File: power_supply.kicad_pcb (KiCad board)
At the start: 2 copper layers, 30 parts, among them J2 Conn_01x03_Socket, J3 Conn_01x02_Socket, J4 Conn_01x03_Socket, U1 LM317_TO-220, U2 LM337_TO220, U3 LM385BZ-1.2, U4 LM385BZ-1.2, U5 LM7812_TO220

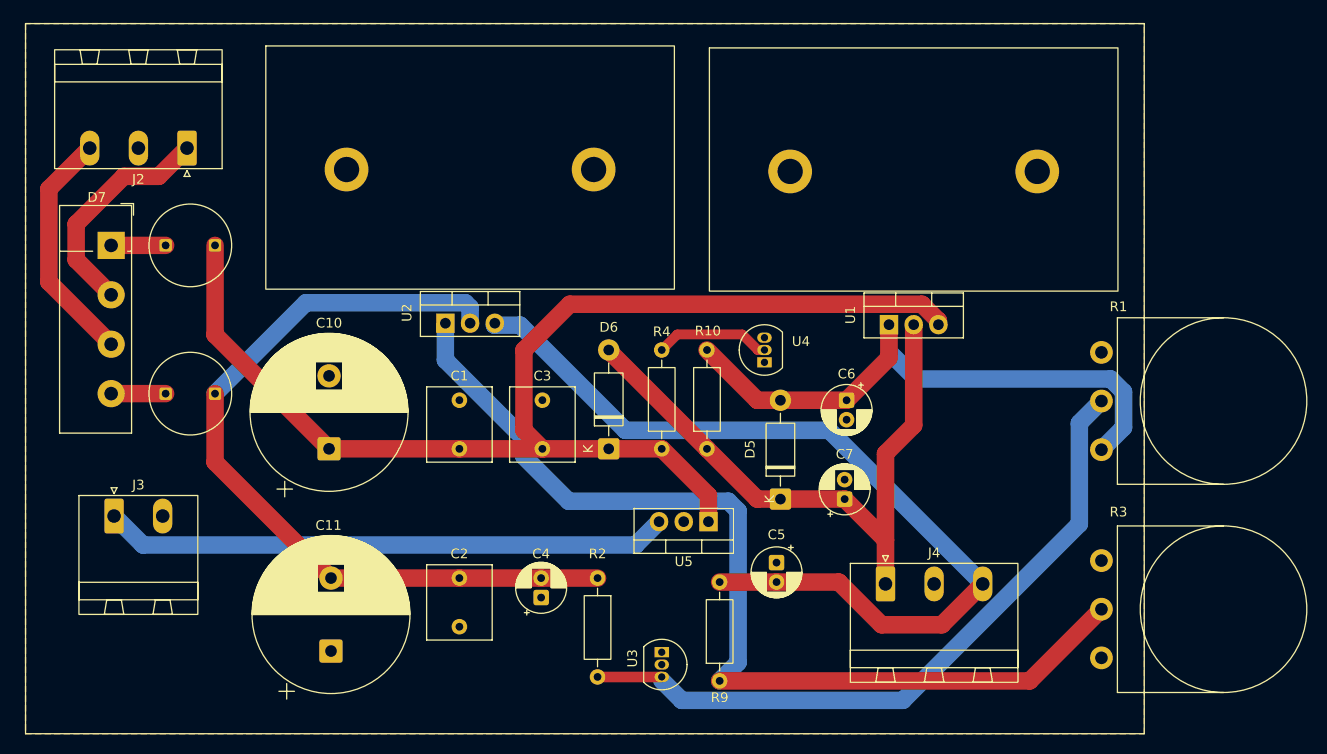
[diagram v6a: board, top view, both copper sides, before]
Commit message: added all traces & vias
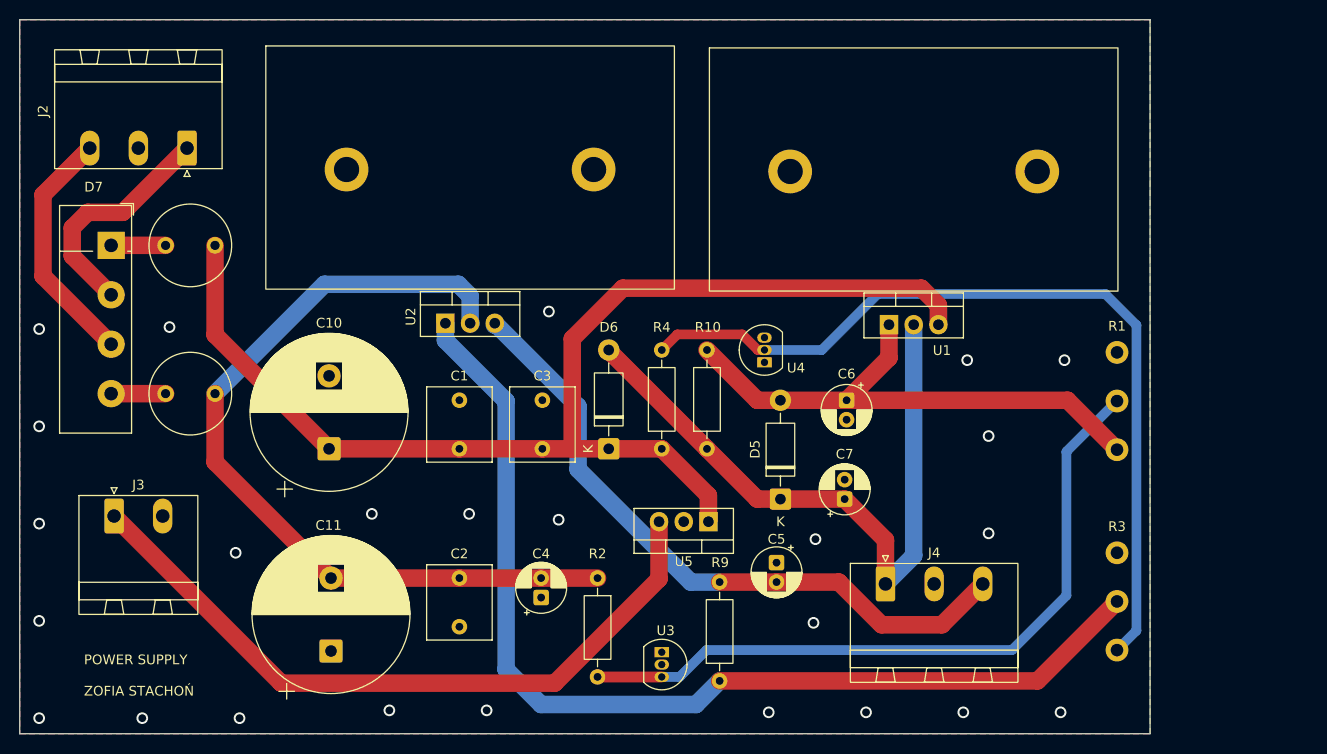
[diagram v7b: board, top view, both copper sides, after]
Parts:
- moved R3 1.79 mm to (196.2, 109.0)
- moved R1 1.60 mm to (196.2, 88.4)
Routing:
- net Net-(U4-K): track 11.9 -> 88.1 mm
- net /0-(-15)V: track 92.0 -> 68.7 mm
- net Net-(J3-Pin_1): track 58.2 -> 73.5 mm
- net Net-(D5-A): track 61.6 -> 56.0 mm
- net Net-(U2-ADJ): track 101.9 -> 106.9 mm
- net /0-15V: track 64.4 -> 68.9 mm
- net Net-(D6-K): track 126.0 -> 123.3 mm
- net Net-(U2-VI): track 83.2 -> 85.6 mm
- net Net-(U3-A): track 71.5 -> 73.8 mm
- net GND: vias 0 -> 25
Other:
- board outline added: 116.2 x 73.4 mm
- board text added: "15k"
- board text added: "POWER SUPPLY ZOFIA STACHOŃ"

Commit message: vinal version completed
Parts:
- HS1, HS2: footprint power_supply_own:RA-T2X-51E -> power_supply_own:RAT2X51E
- moved HS2 25.4 mm to (142.4, 59.4), turned to 180 degrees
- moved HS1 25.2 mm to (187.8, 59.4), turned to 180 degrees
- moved U1 11.2 mm to (172.7, 64.4)
- moved U2 11.0 mm to (127.2, 64.4)
- moved J3 9.40 mm to (92.9, 104.6)
- moved J4 4.94 mm to (168.2, 104.8)
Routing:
- net Net-(D5-A): track 56.0 -> 69.9 mm
- net Net-(U2-ADJ): track 106.9 -> 119.3 mm
- net /0-15V: track 68.9 -> 79.6 mm
- net /0-(-15)V: track 68.7 -> 79.0 mm
- net Net-(D6-K): track 123.3 -> 128.7 mm
- net Net-(J3-Pin_1): track 73.5 -> 69.8 mm
- net Net-(U2-VI): track 85.6 -> 88.5 mm
- net GND: vias 25 -> 21
